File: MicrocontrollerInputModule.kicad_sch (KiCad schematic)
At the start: 46 parts, among them J1 Conn_02x04_Odd_Even, J2 Conn_01x16, J3 Conn_01x10, SW1 KXT3, SW2 KXT3, U1 W25Q16JVUXIQ, U2 RP2040, Y1 12.000MHz

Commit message: Initial reconfiguration for X1 Carbon Gen10 Keyboard module
RP2040 pin assignments are somewhat arbitrary; PCB is not yet routed;
position of framework input module connector is also arbitrary.
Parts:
- removed D6: SK6812MINI-E, InputModule:LED_SK6812MINI-E_PLCC4_3.5x3.5mm_P1.75mm, symbol InputModule:SK6812MINI-E
- removed J2: Conn_01x16, Connector_PinHeader_2.54mm:PinHeader_1x16_P2.54mm_Vertical, symbol Connector_Generic:Conn_01x16
- removed J3: Conn_01x10, Connector_PinHeader_2.54mm:PinHeader_1x10_P2.54mm_Vertical, symbol Connector_Generic:Conn_01x10
- removed R2: 10k, Resistor_SMD:R_0402_1005Metric, symbol Device:R_US
- removed SW1, SW2: KXT3, Button_Switch_SMD:SW_SPST_CK_KXT3, symbol Switch:SW_Push
- added C18: 100nF, Capacitor_SMD:C_0402_1005Metric, symbol Device:C
- added C19: 47uF, Capacitor_SMD:C_0402_1005Metric, symbol Device:C
- added J2: Conn_01x45, symbol Connector_Generic:Conn_01x45
- added R10, R8, R9: 100, Resistor_SMD:R_0402_1005Metric, symbol Device:R_US
- added TP5: BOOTSEL, TestPoint:TestPoint_Pad_D1.0mm, symbol Connector:TestPoint
- added U4: MCP23017_ML, Package_DFN_QFN:QFN-28-1EP_6x6mm_P0.65mm_EP4.25x4.25mm, symbol Interface_Expansion:MCP23017_ML
- R4: value 10k -> 100; now in the parts list
- TP1: value TestPoint -> 3V3
- TP2: value TestPoint -> CLK
- TP3: value TestPoint -> SWD
- TP4: value TestPoint -> GND
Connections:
- net D24 is gone; now on net ~{SLEEP}: U2.36 (GPIO24)
- net LED is gone; now on net ~{HOTKEY}: U2.27 (GPIO16)
- net +3V3: now also C17.2, C18.2, J2.25 (Pin_25), J2.31 (Pin_31), U4.5 (VDD); no longer R4.1
- net +5V: now also C19.2, J2.37 (Pin_37), J2.38 (Pin_38); no longer C17.1
- net GND: now also C17.1, C18.1, C19.1, J2.41 (Pin_41), J2.42 (Pin_42), J2.43 (Pin_43), J2.44 (Pin_44), J2.45 (Pin_45), U4.11 (A0), U4.12 (A1), U4.13 (A2), U4.29 (EP), U4.6 (VSS); no longer C17.2
- net ~{SLEEP}: no longer U2.6 (GPIO4)
- net ~{LED_MICMUTE}: now reaches U2.17 (GPIO14)
- net ~{LED_MICMUTE}: now also R9.1
- net ~{LED_CAPSLOCK}: now reaches U2.18 (GPIO15)
- net ~{LED_CAPSLOCK}: now also R10.1
- net TP4DATA: now reaches U2.28 (GPIO17)
- net TP4DATA: now also J2.32 (Pin_32)
- net ~{TP4_FW_WR_EN}: now reaches U2.32 (GPIO21)
- net ~{TP4_FW_WR_EN}: now also J2.36 (Pin_36)
- net KBD_BL_PWM: now reaches U2.34 (GPIO22)
- net KBD_BL_PWM: now also J2.39 (Pin_39)
- net ~{KBD_BL_DET}: now reaches U2.35 (GPIO23)
- net ~{KBD_BL_DET}: now also J2.40 (Pin_40)
- net SENSE5: now reaches U2.7 (GPIO5)
- net SENSE5: now also J2.12 (Pin_12)
- net ~{HOTKEY}: now reaches R1.1
- net ~{HOTKEY}: now also J2.29 (Pin_29), TP5.1
- net A0: no longer names the net of U2.38 (GPIO26_ADC0)
- net A1: no longer names the net of U2.39 (GPIO27_ADC1)
- net A2: no longer names the net of U2.40 (GPIO28_ADC2)
- net A3: no longer names the net of U2.41 (GPIO29_ADC3)
- net D10 renamed IOEXP_INT
- net IOEXP_INT: now also U4.16 (INTA)
- net D11 renamed ~{IOEXP_RESET}
- net ~{IOEXP_RESET}: now also U4.14 (~{RESET})
- net D12 renamed ~{LED_FNLOCK}
- net ~{LED_FNLOCK}: now also R4.1
- net D13 renamed ~{LED_MUTE}
- net ~{LED_MUTE}: now also R8.1
- net D25: no longer names the net of U2.37 (GPIO25)
- net D4 renamed SENSE6
- net SENSE6: now also J2.3 (Pin_3)
- net D5 renamed SENSE7
- net SENSE7: now also J2.2 (Pin_2)
- net D6 renamed IOEXP_SDA
- net IOEXP_SDA: now also U4.9 (SDA)
- net D9 renamed IOEXP_SCK
- net IOEXP_SCK: now also U4.8 (SCK)
- net MISO renamed ~{TP4ACT}
- net ~{TP4ACT}: now also J2.35 (Pin_35)
- net MOSI renamed TP4CLK
- net TP4CLK: now also J2.34 (Pin_34)
- net RX renamed SENSE1
- net SENSE1: now also J2.6 (Pin_6)
- net SCK renamed TP4RESET
- net TP4RESET: now also J2.33 (Pin_33)
- net SCL renamed SENSE3
- net SENSE3: now also J2.1 (Pin_1)
- net SDA renamed SENSE2
- net SENSE2: now also J2.8 (Pin_8)
- net TX renamed SENSE0
- net SENSE0: now also J2.9 (Pin_9)
- net ~{RESET}: no longer names the net of U2.26 (RUN)
- net ~{RESET}: no longer R4.2
- new net DRV0: J2.7 (Pin_7), U4.17 (GPA0)
- new net DRV1: J2.13 (Pin_13), U4.18 (GPA1)
- new net DRV10: J2.22 (Pin_22), U4.27 (GPB2)
- new net DRV11: J2.24 (Pin_24), U4.28 (GPB3)
- new net DRV12: J2.21 (Pin_21), U4.1 (GPB4)
- new net DRV13: J2.19 (Pin_19), U4.2 (GPB5)
- new net DRV14: J2.4 (Pin_4), U4.3 (GPB6)
- new net DRV15: J2.18 (Pin_18), U4.4 (GPB7)
- new net DRV2: J2.11 (Pin_11), U4.19 (GPA2)
- new net DRV3: J2.14 (Pin_14), U4.20 (GPA3)
- new net DRV4: J2.10 (Pin_10), U4.21 (GPA4)
- new net DRV5: J2.17 (Pin_17), U4.22 (GPA5)
- new net DRV6: J2.15 (Pin_15), U4.23 (GPA6)
- new net DRV7: J2.16 (Pin_16), U4.24 (GPA7)
- new net DRV8: J2.23 (Pin_23), U4.25 (GPB0)
- new net DRV9: J2.20 (Pin_20), U4.26 (GPB1)
- new net SENSE4: J2.5 (Pin_5), U2.6 (GPIO4)
- new net ~{LED_CAPSLOCK_R}: J2.30 (Pin_30), R10.2
- new net ~{LED_FNLOCK_R}: J2.26 (Pin_26), R4.2
- new net ~{LED_MICMUTE_R}: J2.28 (Pin_28), R9.2
- new net ~{LED_MUTE_R}: J2.27 (Pin_27), R8.2
- no-connect marks 8 -> 2
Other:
- note added: "LED Current-Limiting"
- note removed: "Feather Header"
- company: Framework Computer Inc -> C. Scott Ananian and Framework Computer Inc
- title: Microcontroller Input Module -> X1 Carbon Gen10 Keyboard Interface

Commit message: First complete version, fully routed
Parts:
- removed J2: Conn_01x45, symbol Connector_Generic:Conn_01x45
- added C20: 100nF, Capacitor_SMD:C_0402_1005Metric, symbol Device:C
- added J3: IPEX 20655-045E-01, 20655-045E-01:IPEX_20655-045E-01, symbol 20655-045E-01:20655-045E-01
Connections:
- net +3V3: now also C20.1, J3.15, J3.21
- net +5V: now also J3.8, J3.9
- net DRV0: now also U4.3 (GPB6), J3.39; no longer U4.17 (GPA0)
- net DRV1: now also U4.28 (GPB3), J3.33; no longer U4.18 (GPA1)
- net DRV10: now also U4.19 (GPA2), J3.24; no longer U4.27 (GPB2)
- net DRV11: now also U4.17 (GPA0), J3.22; no longer U4.28 (GPB3)
- net DRV12: now also U4.20 (GPA3), J3.25; no longer U4.1 (GPB4)
- net DRV13: now also U4.22 (GPA5), J3.27; no longer U4.2 (GPB5)
- net DRV14: now also U4.4 (GPB7), J3.42; no longer U4.3 (GPB6)
- net DRV15: now also U4.23 (GPA6), J3.28; no longer U4.4 (GPB7)
- net DRV2: now also U4.1 (GPB4), J3.35; no longer U4.19 (GPA2)
- net DRV3: now also U4.27 (GPB2), J3.32; no longer U4.20 (GPA3)
- net DRV4: now also U4.2 (GPB5), J3.36; no longer U4.21 (GPA4)
- net DRV5: now also U4.24 (GPA7), J3.29; no longer U4.22 (GPA5)
- net DRV6: now also U4.26 (GPB1), J3.31; no longer U4.23 (GPA6)
- net DRV7: now also U4.25 (GPB0), J3.30; no longer U4.24 (GPA7)
- net DRV8: now also U4.18 (GPA1), J3.23; no longer U4.25 (GPB0)
- net DRV9: now also U4.21 (GPA4), J3.26; no longer U4.26 (GPB1)
- net GND: now also C20.2, J3.1, J3.2, J3.3, J3.4, J3.5, J3.LOCK1 (LOCK), J3.LOCK2 (LOCK), J3.S1 (SHIELD), J3.S2 (SHIELD), J3.S3 (SHIELD), J3.S4 (SHIELD)
- net IOEXP_INT: now also U2.5 (GPIO3); no longer U2.13 (GPIO10)
- net IOEXP_SCK: now also U2.3 (GPIO1); no longer U2.12 (GPIO9)
- net IOEXP_SDA: now also U2.2 (GPIO0); no longer U2.11 (GPIO8)
- net KBD_BL_PWM: now also U2.14 (GPIO11), J3.7; no longer U2.34 (GPIO22)
- net SENSE0: now also U2.28 (GPIO17), J3.37; no longer U2.2 (GPIO0)
- net SENSE1: now also U2.30 (GPIO19), J3.40; no longer U2.3 (GPIO1)
- net SENSE2: now also U2.29 (GPIO18), J3.38; no longer U2.4 (GPIO2)
- net SENSE3: now also U2.34 (GPIO22), J3.45; no longer U2.5 (GPIO3)
- net SENSE4: now also U2.32 (GPIO21), J3.41; no longer U2.6 (GPIO4)
- net SENSE5: now also U2.27 (GPIO16), J3.34; no longer U2.7 (GPIO5)
- net SENSE6: now also U2.35 (GPIO23), J3.43; no longer U2.8 (GPIO6)
- net SENSE7: now also U2.31 (GPIO20), J3.44; no longer U2.9 (GPIO7)
- net TP4CLK: now also U2.8 (GPIO6), J3.12; no longer U2.30 (GPIO19)
- net TP4DATA: now also U2.9 (GPIO7), J3.14; no longer U2.28 (GPIO17)
- net TP4RESET: now also U2.16 (GPIO13), J3.13; no longer U2.29 (GPIO18)
- net ~{HOTKEY}: now also U2.17 (GPIO14), J3.17; no longer U2.27 (GPIO16)
- net ~{IOEXP_RESET}: now also U2.4 (GPIO2); no longer U2.14 (GPIO11)
- net ~{KBD_BL_DET}: now also U2.36 (GPIO24), J3.6; no longer U2.35 (GPIO23)
- net ~{LED_CAPSLOCK_R}: now also J3.16
- net ~{LED_CAPSLOCK}: now also U2.11 (GPIO8); no longer U2.18 (GPIO15)
- net ~{LED_FNLOCK_R}: now also J3.20
- net ~{LED_FNLOCK}: now also U2.13 (GPIO10); no longer U2.15 (GPIO12)
- net ~{LED_MICMUTE_R}: now also J3.18
- net ~{LED_MICMUTE}: now also U2.12 (GPIO9); no longer U2.17 (GPIO14)
- net ~{LED_MUTE_R}: now also J3.19
- net ~{LED_MUTE}: now also U2.18 (GPIO15); no longer U2.16 (GPIO13)
- net ~{SLEEP}: now also U2.6 (GPIO4); no longer U2.36 (GPIO24)
- net ~{TP4ACT}: now also U2.15 (GPIO12), J3.11; no longer U2.31 (GPIO20)
- net ~{TP4_FW_WR_EN}: now also U2.7 (GPIO5), J3.10; no longer U2.32 (GPIO21)
- no-connect marks 2 -> 7
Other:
- note added: "Top Entry, so pins are reversed"
- moved on the sheet: C17, C18, C19, U4

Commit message: Renumber components, tidy up silkscreen
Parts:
- renumbered C3 to C1, C8 to C10, C9 to C11, C10 to C12, C11 to C13, C12 to C14, C20 to C15, C13 to C16, C14 to C17, C1 to C2, C17 to C20, C2 to C3, C15 to C5, C5 to C6, C6 to C7, C16 to C8, C7 to C9, J3 to J2, R7 to R2, R5 to R4, R6 to R5, R4 to R6, R8 to R7, R9 to R8, R10 to R9, TP5 to TP1, TP1 to TP2, TP2 to TP3, TP3 to TP4, TP4 to TP5, U4 to U3

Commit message: Update README; change C19 to an 0603 cap; improve ground plane connectivity
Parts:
- C19: footprint Capacitor_SMD:C_0402_1005Metric -> Capacitor_SMD:C_0603_1608Metric
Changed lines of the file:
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@@
       (effects (font (size 1.27 1.27)) (justify left))
     )
-    (property "Footprint" "Capacitor_SMD:C_0402_1005Metric" (at 246.38 132.3848 0)
+    (property "Footprint" "Capacitor_SMD:C_0603_1608Metric" (at 246.38 132.3848 0)
       (effects (font (size 1.27 1.27)) hide)
     )

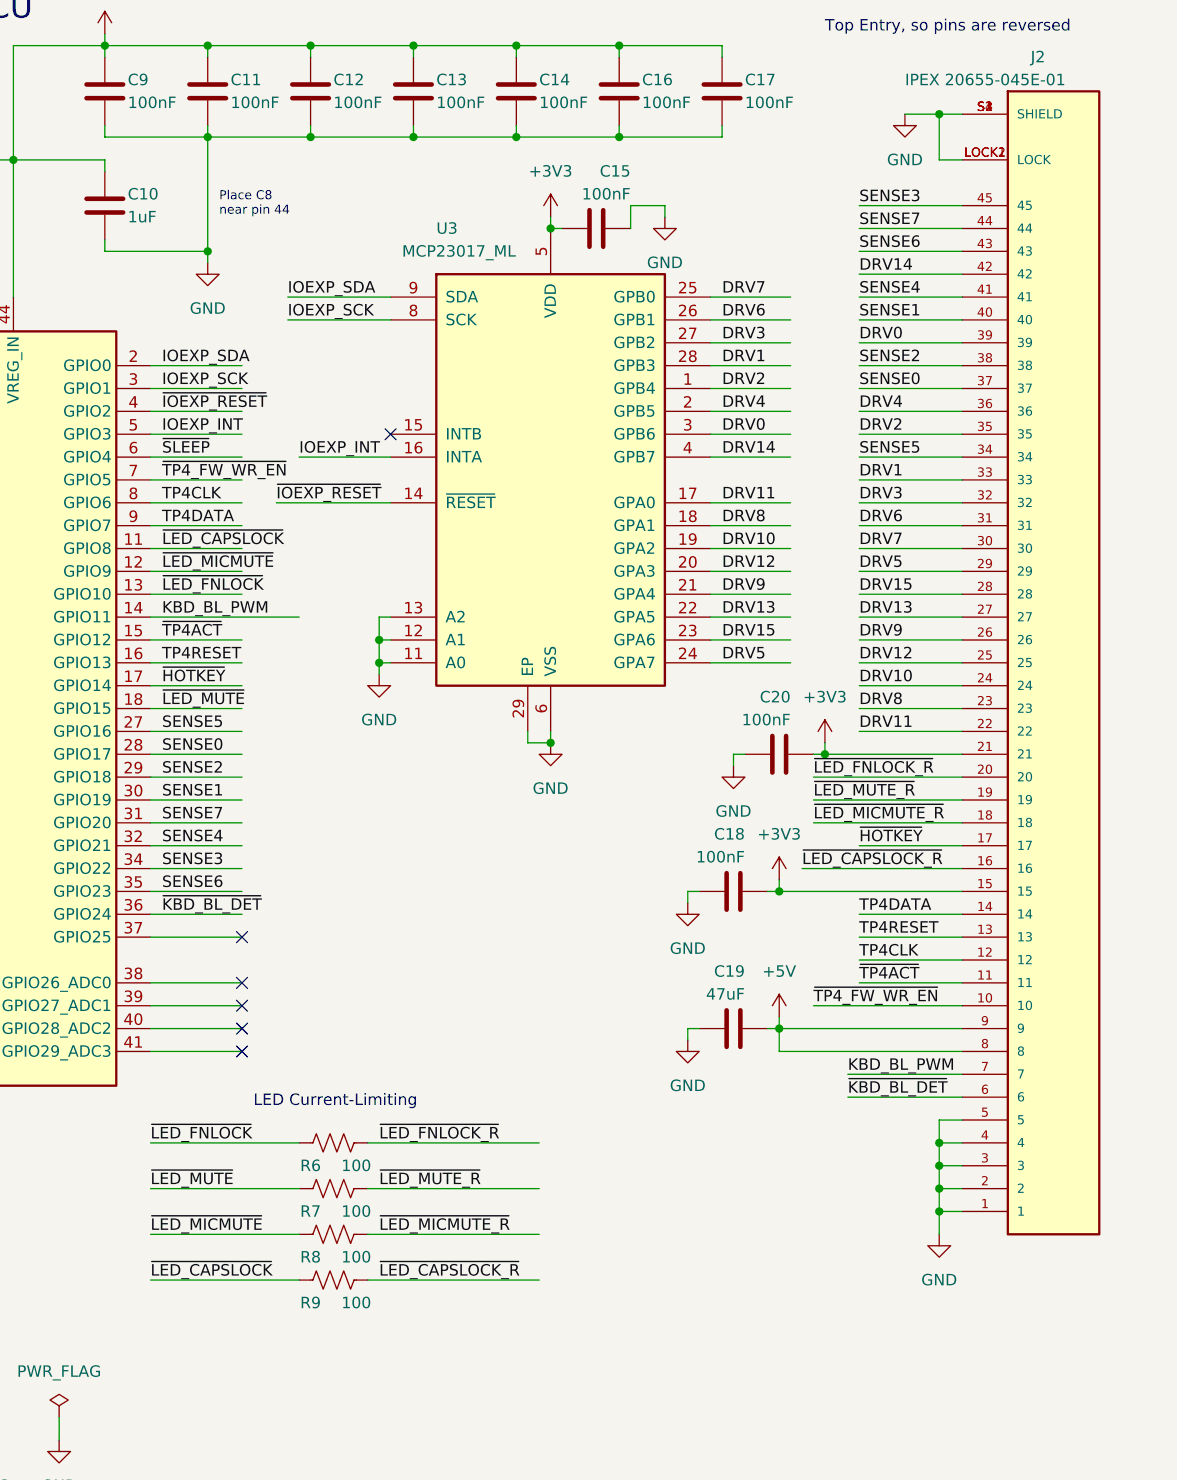
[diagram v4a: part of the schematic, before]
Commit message: Swap TP4CLK and TP4DATA to handle PIO requirements
The current RP2040 PS/2 driver in:

https://github.com/qmk/qmk_firmware/blob/master/platforms/chibios/drivers/vendor/RP/RP2040/ps2_vendor.c#L24

requires that PS2_DATA_PIN is the one *before* PS2_CLOCK_PIN, so swap our
GPIO assignments to match.
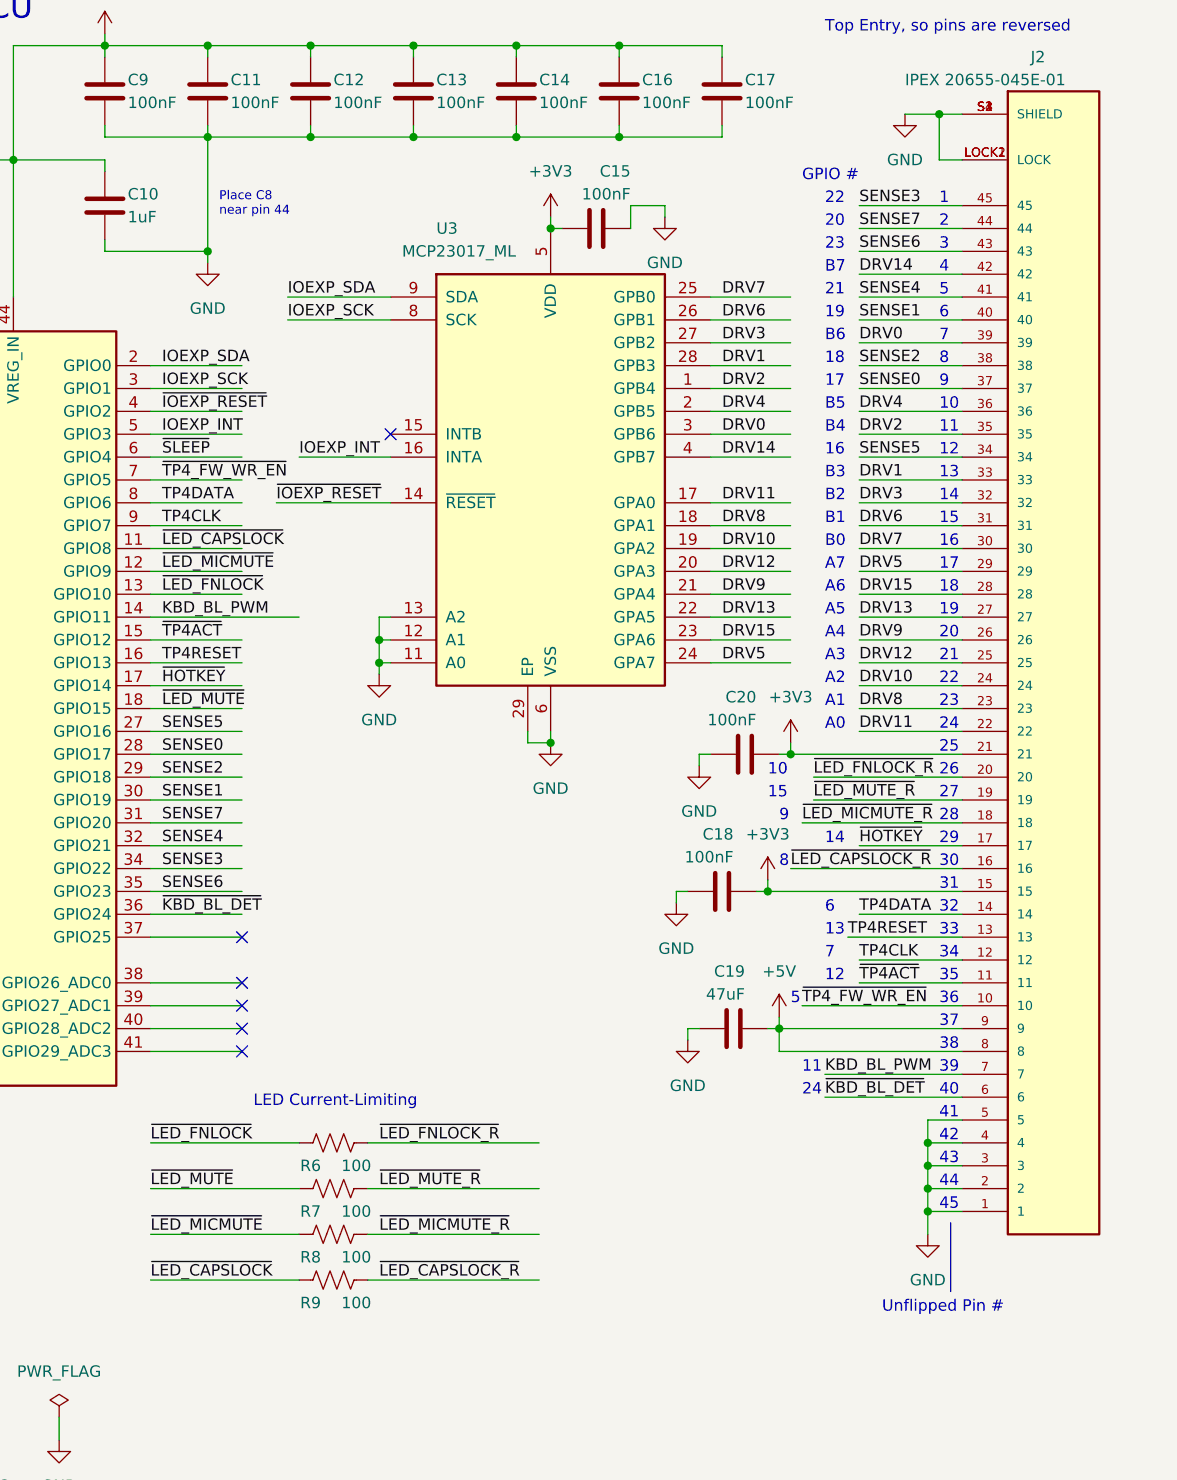
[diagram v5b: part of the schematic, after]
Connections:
- net TP4CLK: now also U2.9 (GPIO7); no longer U2.8 (GPIO6)
- net TP4DATA: now also U2.8 (GPIO6); no longer U2.9 (GPIO7)
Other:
- note added: "1"
- note added: "10"
- note added: "11"
- note added: "12"
- note added: "13"
- note added: "14"
- note added: "15"
- note added: "16"
- note added: "17"
- note added: "18"
- note added: "19"
- note added: "2"
- note added: "20"
- note added: "21"
- note added: "22"
- note added: "23"
- note added: "24"
- note added: "25"
- note added: "26"
- note added: "27"
- note added: "28"
- note added: "29"
- note added: "3"
- note added: "30"
- note added: "31"
- note added: "32"
- note added: "33"
- note added: "34"
- note added: "35"
- note added: "36"
- note added: "37"
- note added: "38"
- note added: "39"
- note added: "4"
- note added: "40"
- note added: "41"
- note added: "42"
- note added: "43"
- note added: "44"
- note added: "45"
- note added: "5"
- note added: "6"
- note added: "7"
- note added: "8"
- note added: "9"
- note added: "A0"
- note added: "A1"
- note added: "A2"
- note added: "A3"
- note added: "A4"
- note added: "A5"
- note added: "A6"
- note added: "A7"
- note added: "B0"
- note added: "B1"
- note added: "B2"
- note added: "B3"
- note added: "B4"
- note added: "B5"
- note added: "B6"
- note added: "B7"
- note added: "GPIO #"
- note added: "Unflipped Pin #"
- moved on the sheet: C18, C20
